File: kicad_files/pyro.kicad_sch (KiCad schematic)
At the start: 12 parts, among them J11 IGN_1, J12 IGN_2, Q1 AO3400A, Q2 AO3400A

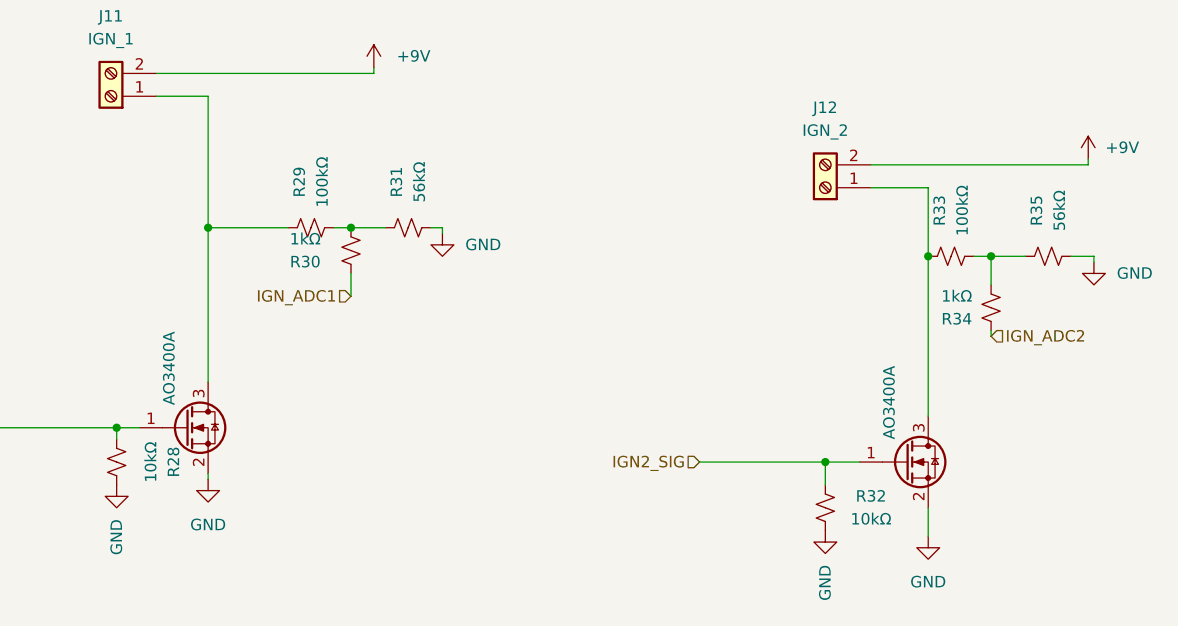
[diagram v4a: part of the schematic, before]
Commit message: fix schem for buck conv
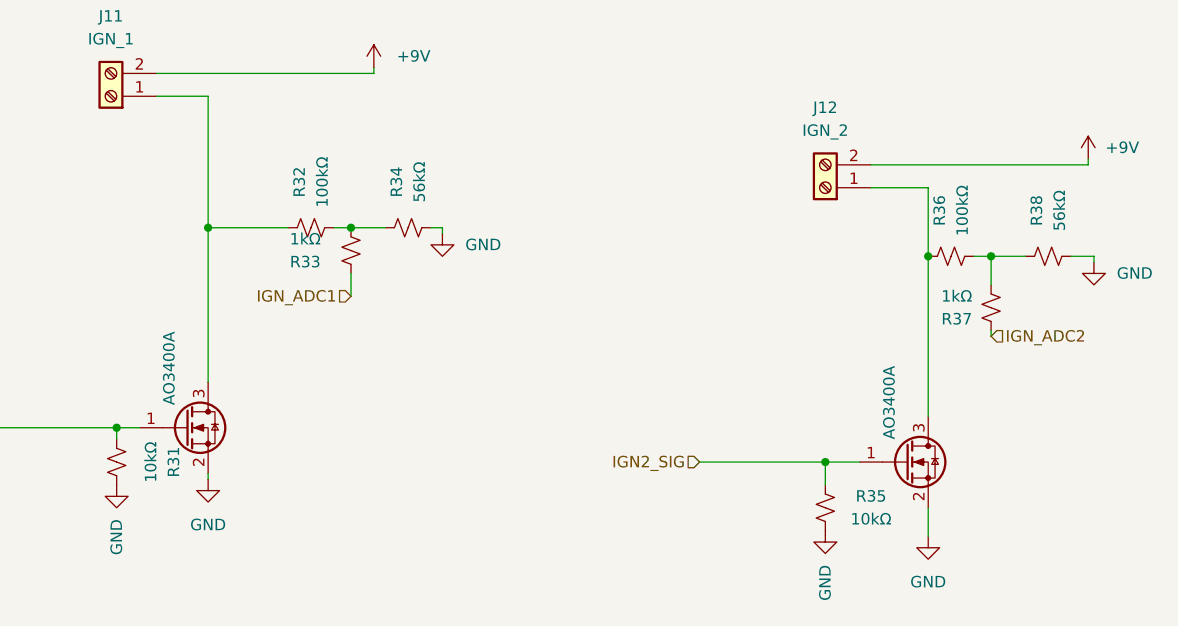
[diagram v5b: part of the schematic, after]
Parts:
- renumbered R28 to R31, R29 to R32, R30 to R33, R31 to R34, R32 to R35, R33 to R36, R34 to R37, R35 to R38
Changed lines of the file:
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@@
 		(in_pos_files yes)
 		(dnp no)
-		(property "Reference" "R29"
+		(property "Reference" "R32"
 			(at 146.685 81.915 0)
 			(show_name no)
@@
 			(project "versorlite"
 				(path "/1a230af0-0a74-48f7-8607-b087121dda49/f02bd2f9-723f-45ac-a652-42be6cba2a93"
-					(reference "R29")
+					(reference "R32")
 					(unit 1)
 				)
@@
 		(dnp no)
 		(fields_autoplaced yes)
-		(property "Reference" "#PWR094"
+		(property "Reference" "#PWR093"
 			(at 126.365 121.92 0)
 			(hide yes)
@@
 			(project "versorlite"
 				(path "/1a230af0-0a74-48f7-8607-b087121dda49/f02bd2f9-723f-45ac-a652-42be6cba2a93"
-					(reference "#PWR094")
+					(reference "#PWR093")
 					(unit 1)
 				)
@@
 		(dnp no)
 		(fields_autoplaced yes)
-		(property "Reference" "#PWR097"
+		(property "Reference" "#PWR096"
 			(at 162.56 93.98 0)
 			(hide yes)
@@
 			(project "versorlite"
 				(path "/1a230af0-0a74-48f7-8607-b087121dda49/f02bd2f9-723f-45ac-a652-42be6cba2a93"
-					(reference "#PWR097")
+					(reference "#PWR096")
 					(unit 1)
 				)
@@
 		(in_pos_files yes)
 		(dnp no)
-		(property "Reference" "R35"
+		(property "Reference" "R38"
 			(at 228.6 85.09 0)
 			(show_name no)
@@
 			(project "versorlite"
 				(path "/1a230af0-0a74-48f7-8607-b087121dda49/f02bd2f9-723f-45ac-a652-42be6cba2a93"
-					(reference "R35")
+					(reference "R38")
 					(unit 1)
 				)
@@
 		(dnp no)
 		(fields_autoplaced yes)
-		(property "Reference" "#PWR099"
+		(property "Reference" "#PWR098"
 			(at 216.535 127.635 0)
 			(hide yes)
@@
 			(project "versorlite"
 				(path "/1a230af0-0a74-48f7-8607-b087121dda49/f02bd2f9-723f-45ac-a652-42be6cba2a93"
-					(reference "#PWR099")
+					(reference "#PWR098")
 					(unit 1)
 				)
@@
 		(dnp no)
 		(fields_autoplaced yes)
-		(property "Reference" "#PWR096"
+		(property "Reference" "#PWR095"
 			(at 154.94 73.025 0)
 			(hide yes)
@@
 			(project "versorlite"
 				(path "/1a230af0-0a74-48f7-8607-b087121dda49/f02bd2f9-723f-45ac-a652-42be6cba2a93"
-					(reference "#PWR096")
+					(reference "#PWR095")
 					(unit 1)
 				)
@@
 		(dnp no)
 		(fields_autoplaced yes)
-		(property "Reference" "#PWR095"
+		(property "Reference" "#PWR094"
 			(at 136.525 121.285 0)
 			(hide yes)
@@
 			(project "versorlite"
 				(path "/1a230af0-0a74-48f7-8607-b087121dda49/f02bd2f9-723f-45ac-a652-42be6cba2a93"
-					(reference "#PWR095")
+					(reference "#PWR094")
 					(unit 1)
 				)
@@
 		(dnp no)
 		(fields_autoplaced yes)
-		(property "Reference" "#PWR098"
+		(property "Reference" "#PWR097"
 			(at 205.105 127 0)
 			(hide yes)
@@
 			(project "versorlite"
 				(path "/1a230af0-0a74-48f7-8607-b087121dda49/f02bd2f9-723f-45ac-a652-42be6cba2a93"
-					(reference "#PWR098")
+					(reference "#PWR097")
 					(unit 1)
 				)
@@
 		(in_pos_files yes)
 		(dnp no)
-		(property "Reference" "R33"
+		(property "Reference" "R36"
 			(at 217.805 85.09 0)
 			(show_name no)
@@
 			(project "versorlite"
 				(path "/1a230af0-0a74-48f7-8607-b087121dda49/f02bd2f9-723f-45ac-a652-42be6cba2a93"
-					(reference "R33")
+					(reference "R36")
 					(unit 1)
 				)
@@
 		(in_pos_files yes)
 		(dnp no)
-		(property "Reference" "R34"
+		(property "Reference" "R37"
 			(at 219.71 97.155 0)
 			(show_name no)
@@
 			(project "versorlite"
 				(path "/1a230af0-0a74-48f7-8607-b087121dda49/f02bd2f9-723f-45ac-a652-42be6cba2a93"
-					(reference "R34")
+					(reference "R37")
 					(unit 1)
 				)
@@
 		(in_pos_files yes)
 		(dnp no)
-		(property "Reference" "R31"
+		(property "Reference" "R34"
 			(at 157.48 81.915 0)
 			(show_name no)
@@
 			(project "versorlite"
 				(path "/1a230af0-0a74-48f7-8607-b087121dda49/f02bd2f9-723f-45ac-a652-42be6cba2a93"
-					(reference "R31")
+					(reference "R34")
 					(unit 1)
 				)
@@
 		(in_pos_files yes)
 		(dnp no)
-		(property "Reference" "R32"
+		(property "Reference" "R35"
 			(at 210.185 116.84 0)
 			(show_name no)
@@
 			(project "versorlite"
 				(path "/1a230af0-0a74-48f7-8607-b087121dda49/f02bd2f9-723f-45ac-a652-42be6cba2a93"
-					(reference "R32")
+					(reference "R35")
 					(unit 1)
 				)
@@
 		(in_pos_files yes)
 		(dnp no)
-		(property "Reference" "R30"
+		(property "Reference" "R33"
 			(at 147.32 90.805 0)
 			(show_name no)
@@
 			(project "versorlite"
 				(path "/1a230af0-0a74-48f7-8607-b087121dda49/f02bd2f9-723f-45ac-a652-42be6cba2a93"
-					(reference "R30")
+					(reference "R33")
 					(unit 1)
 				)
@@
 		(dnp no)
 		(fields_autoplaced yes)
-		(property "Reference" "#PWR0101"
+		(property "Reference" "#PWR099"
 			(at 234.315 83.185 0)
 			(hide yes)
@@
 			(project "versorlite"
 				(path "/1a230af0-0a74-48f7-8607-b087121dda49/f02bd2f9-723f-45ac-a652-42be6cba2a93"
-					(reference "#PWR0101")
+					(reference "#PWR099")
 					(unit 1)
 				)
@@
 		(in_pos_files yes)
 		(dnp no)
-		(property "Reference" "R28"
+		(property "Reference" "R31"
 			(at 132.715 113.03 90)
 			(show_name no)
@@
 			(project "versorlite"
 				(path "/1a230af0-0a74-48f7-8607-b087121dda49/f02bd2f9-723f-45ac-a652-42be6cba2a93"
-					(reference "R28")
-					(unit 1)
-				)
+					(reference "R31")
+					(unit 1)
+				)
